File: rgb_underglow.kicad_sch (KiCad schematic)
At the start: 33 parts, among them U8 74AHCT1G125

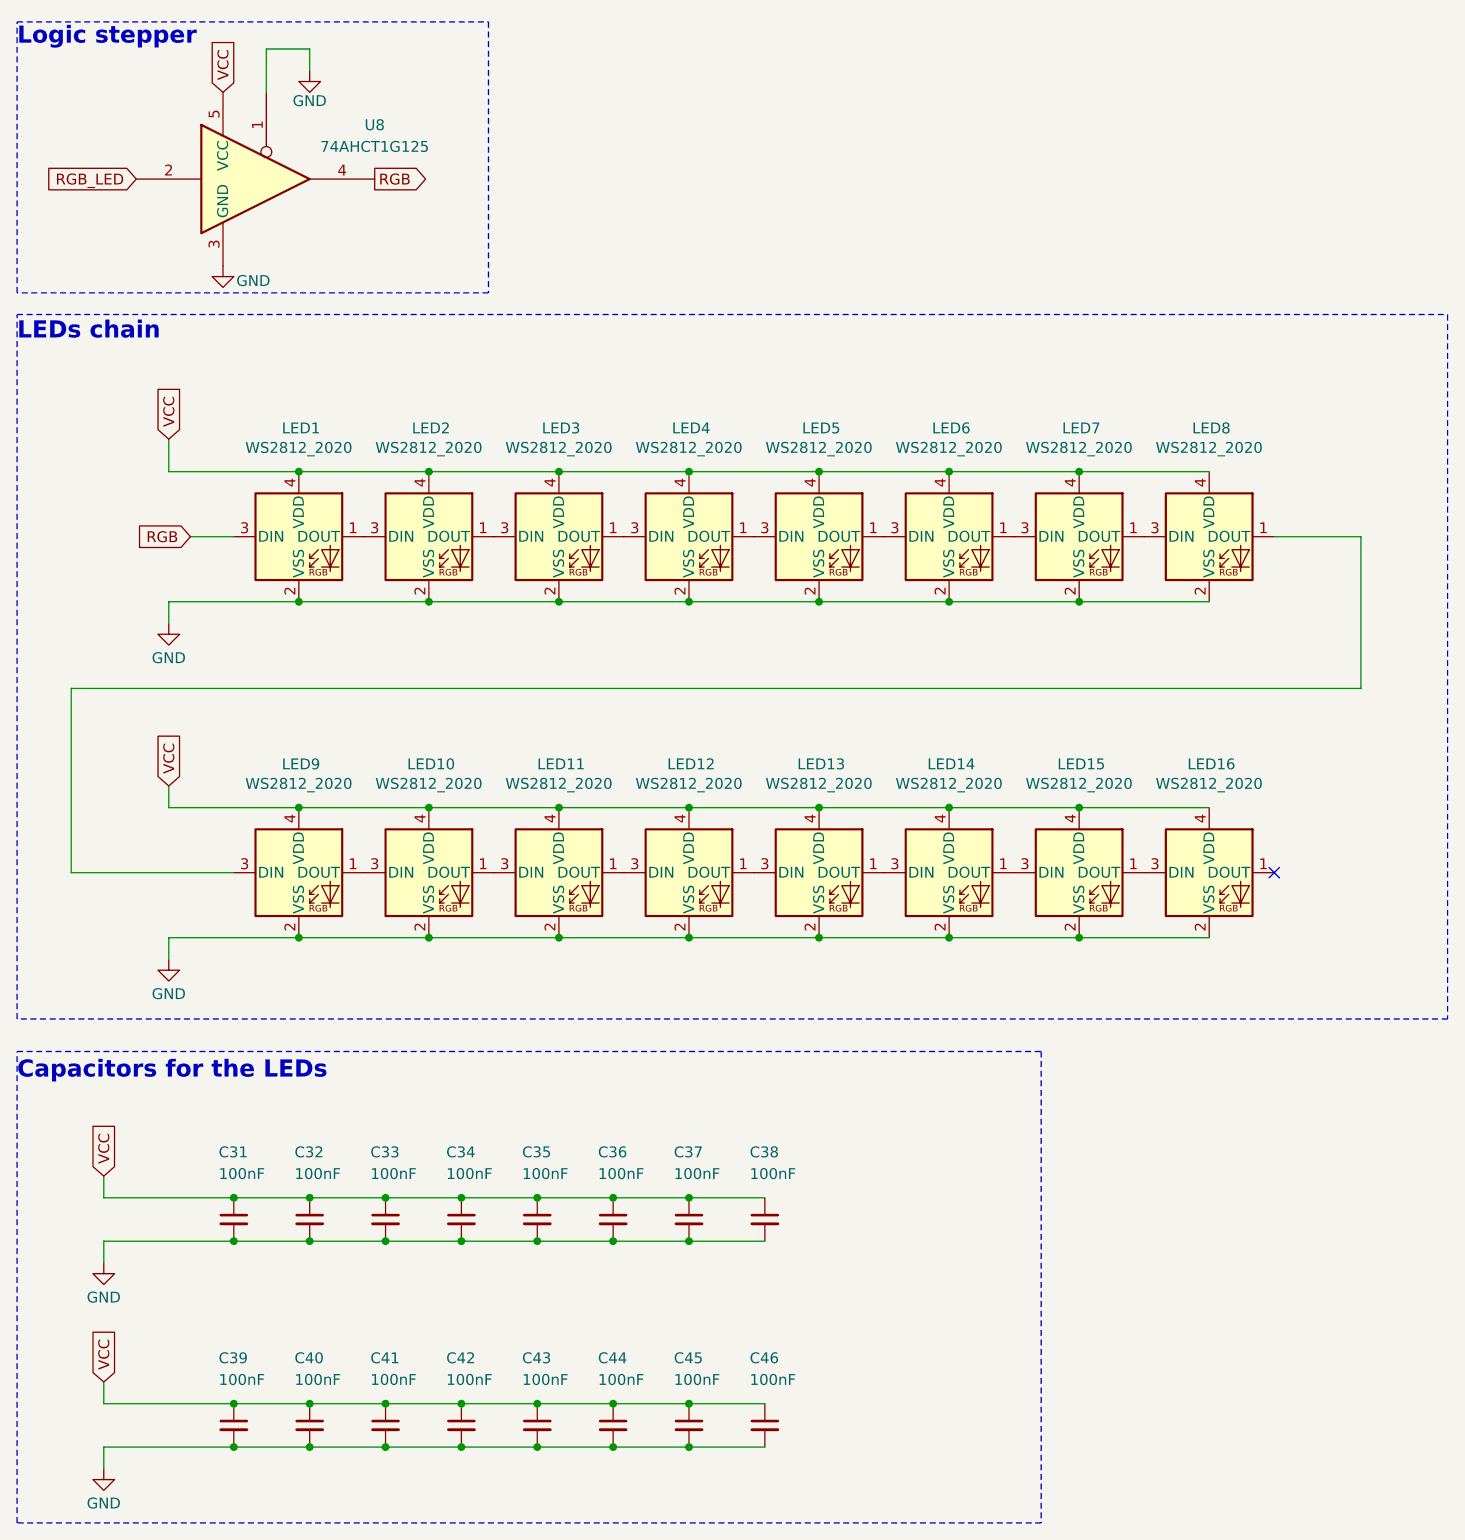
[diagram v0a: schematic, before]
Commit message: Changed USB type-A and LED parts
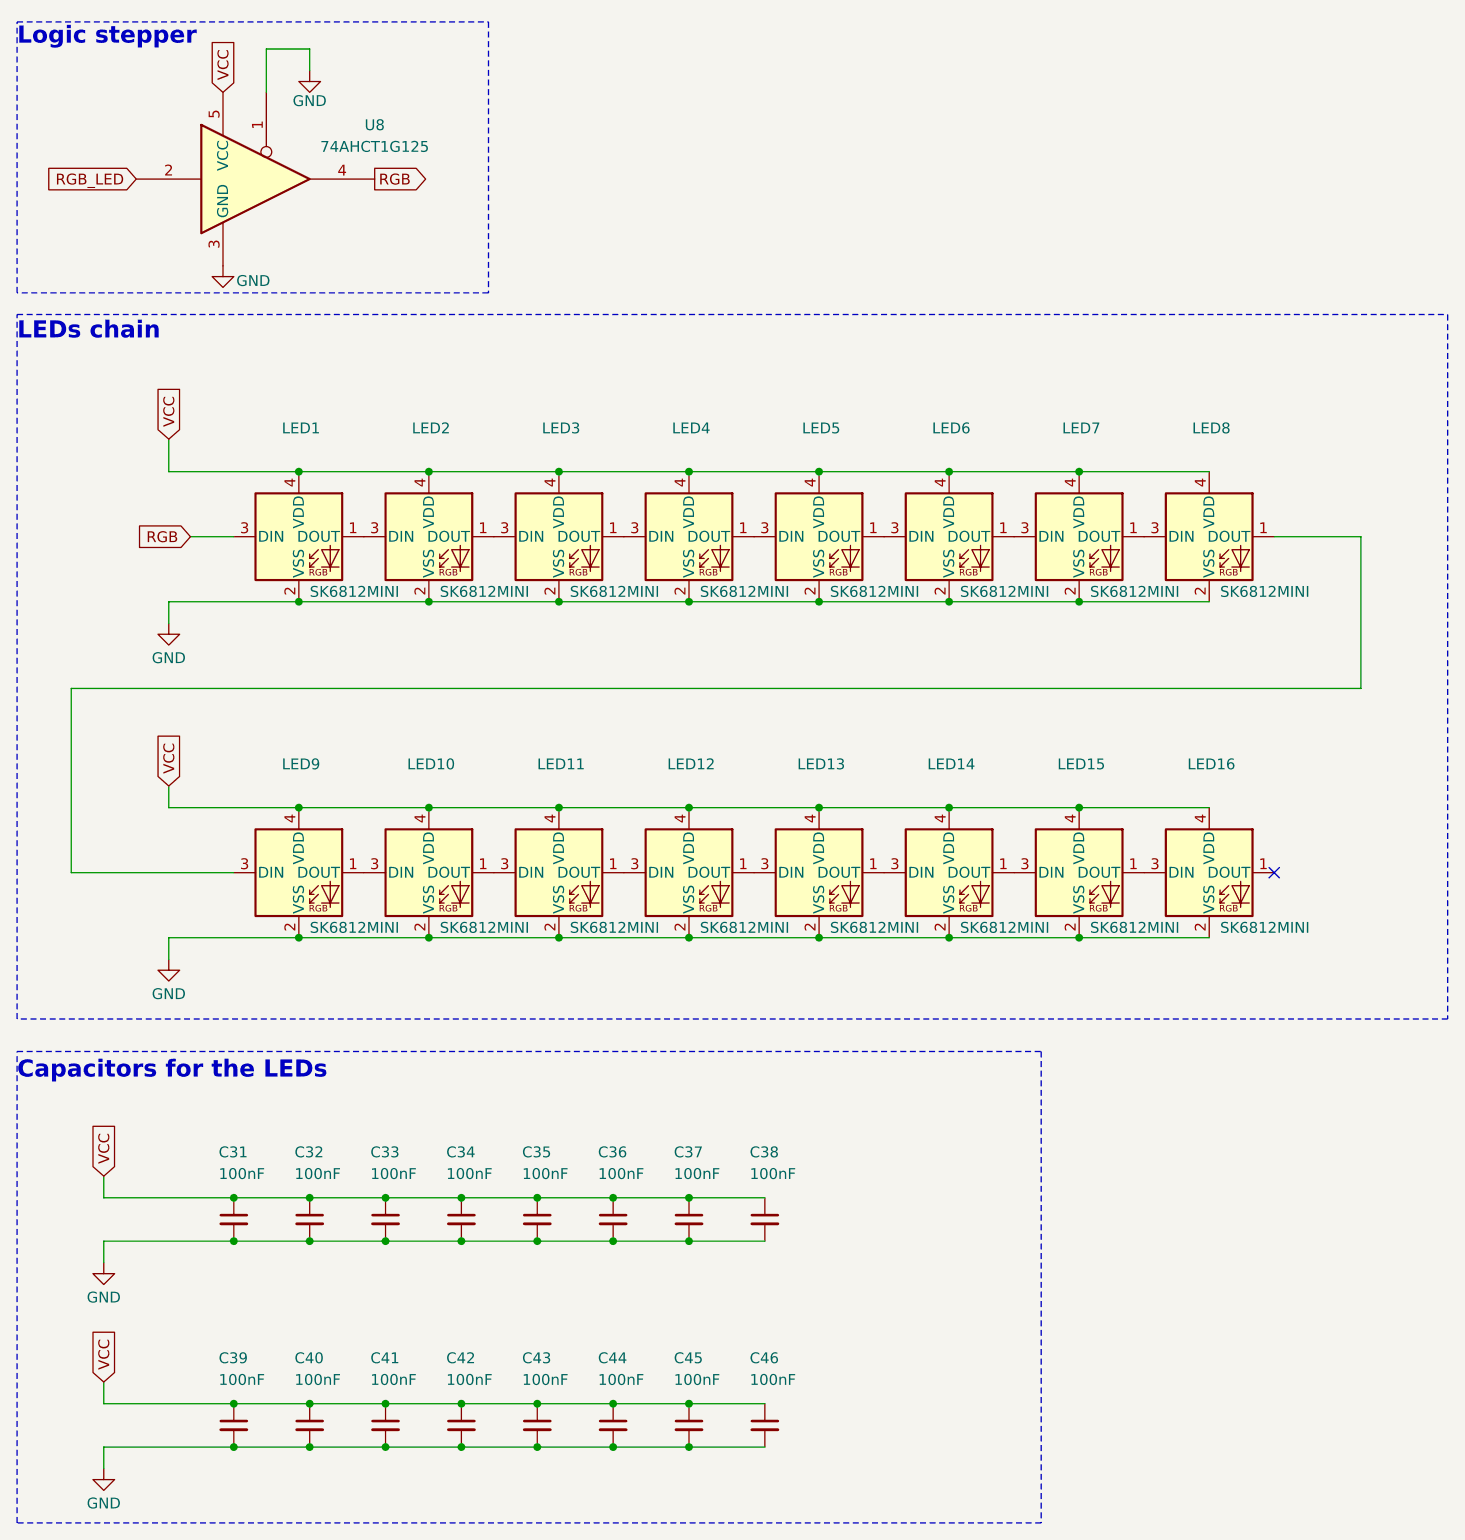
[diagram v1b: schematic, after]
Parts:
- LED1, LED10, LED11, LED12, LED13, LED14, LED15, LED16, LED2, LED3, LED4, LED5, LED6, LED7, LED8, LED9: value WS2812_2020 -> SK6812MINI; footprint PCM_marbastlib-various:LED_WS2812_2020 -> LED_SMD:LED_SK6812MINI_PLCC4_3.5x3.5mm_P1.75mm; symbol PCM_marbastlib-various:WS2812_2020 -> LED:SK6812MINI

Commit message: checking phase
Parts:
- LED1, LED10, LED11, LED12, LED13, LED14, LED15, LED16, LED2, LED3, LED4, LED5, LED6, LED7, LED8, LED9: footprint LED_SMD:LED_SK6812MINI_PLCC4_3.5x3.5mm_P1.75mm -> LED_SK6812MINI_HS:LED_SK6812MINI_HAND_SOLDER_3.5x3.5mm_P1.75mm
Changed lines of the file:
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@@
 			)
 		)
-		(property "Footprint" "LED_SMD:LED_SK6812MINI_PLCC4_3.5x3.5mm_P1.75mm"
+		(property "Footprint" "LED_SK6812MINI_HS:LED_SK6812MINI_HAND_SOLDER_3.5x3.5mm_P1.75mm"
 			(at 139.7 121.92 0)
 			(effects
@@
 			)
 		)
-		(property "Footprint" "LED_SMD:LED_SK6812MINI_PLCC4_3.5x3.5mm_P1.75mm"
+		(property "Footprint" "LED_SK6812MINI_HS:LED_SK6812MINI_HAND_SOLDER_3.5x3.5mm_P1.75mm"
 			(at 93.98 82.55 0)
 			(effects
@@
 			)
 		)
-		(property "Footprint" "LED_SMD:LED_SK6812MINI_PLCC4_3.5x3.5mm_P1.75mm"
+		(property "Footprint" "LED_SK6812MINI_HS:LED_SK6812MINI_HAND_SOLDER_3.5x3.5mm_P1.75mm"
 			(at 48.26 121.92 0)
 			(effects
@@
 			)
 		)
-		(property "Footprint" "LED_SMD:LED_SK6812MINI_PLCC4_3.5x3.5mm_P1.75mm"
+		(property "Footprint" "LED_SK6812MINI_HS:LED_SK6812MINI_HAND_SOLDER_3.5x3.5mm_P1.75mm"
 			(at 109.22 82.55 0)
 			(effects
@@
 			)
 		)
-		(property "Footprint" "LED_SMD:LED_SK6812MINI_PLCC4_3.5x3.5mm_P1.75mm"
+		(property "Footprint" "LED_SK6812MINI_HS:LED_SK6812MINI_HAND_SOLDER_3.5x3.5mm_P1.75mm"
 			(at 63.5 121.92 0)
 			(effects
@@
 			)
 		)
-		(property "Footprint" "LED_SMD:LED_SK6812MINI_PLCC4_3.5x3.5mm_P1.75mm"
+		(property "Footprint" "LED_SK6812MINI_HS:LED_SK6812MINI_HAND_SOLDER_3.5x3.5mm_P1.75mm"
 			(at 93.98 121.92 0)
 			(effects
@@
 			)
 		)
-		(property "Footprint" "LED_SMD:LED_SK6812MINI_PLCC4_3.5x3.5mm_P1.75mm"
+		(property "Footprint" "LED_SK6812MINI_HS:LED_SK6812MINI_HAND_SOLDER_3.5x3.5mm_P1.75mm"
 			(at 154.94 82.55 0)
 			(effects
@@
 			)
 		)
-		(property "Footprint" "LED_SMD:LED_SK6812MINI_PLCC4_3.5x3.5mm_P1.75mm"
+		(property "Footprint" "LED_SK6812MINI_HS:LED_SK6812MINI_HAND_SOLDER_3.5x3.5mm_P1.75mm"
 			(at 124.46 82.55 0)
 			(effects
@@
 			)
 		)
-		(property "Footprint" "LED_SMD:LED_SK6812MINI_PLCC4_3.5x3.5mm_P1.75mm"
+		(property "Footprint" "LED_SK6812MINI_HS:LED_SK6812MINI_HAND_SOLDER_3.5x3.5mm_P1.75mm"
 			(at 109.22 121.92 0)
 			(effects
@@
 			)
 		)
-		(property "Footprint" "LED_SMD:LED_SK6812MINI_PLCC4_3.5x3.5mm_P1.75mm"
+		(property "Footprint" "LED_SK6812MINI_HS:LED_SK6812MINI_HAND_SOLDER_3.5x3.5mm_P1.75mm"
 			(at 48.26 82.55 0)
 			(effects
@@
 			)
 		)
-		(property "Footprint" "LED_SMD:LED_SK6812MINI_PLCC4_3.5x3.5mm_P1.75mm"
+		(property "Footprint" "LED_SK6812MINI_HS:LED_SK6812MINI_HAND_SOLDER_3.5x3.5mm_P1.75mm"
 			(at 124.46 121.92 0)
 			(effects
@@
 			)
 		)
-		(property "Footprint" "LED_SMD:LED_SK6812MINI_PLCC4_3.5x3.5mm_P1.75mm"
+		(property "Footprint" "LED_SK6812MINI_HS:LED_SK6812MINI_HAND_SOLDER_3.5x3.5mm_P1.75mm"
 			(at 63.5 82.55 0)
 			(effects
@@
 			)
 		)
-		(property "Footprint" "LED_SMD:LED_SK6812MINI_PLCC4_3.5x3.5mm_P1.75mm"
+		(property "Footprint" "LED_SK6812MINI_HS:LED_SK6812MINI_HAND_SOLDER_3.5x3.5mm_P1.75mm"
 			(at 154.94 121.92 0)
 			(effects
@@
 			)
 		)
-		(property "Footprint" "LED_SMD:LED_SK6812MINI_PLCC4_3.5x3.5mm_P1.75mm"
+		(property "Footprint" "LED_SK6812MINI_HS:LED_SK6812MINI_HAND_SOLDER_3.5x3.5mm_P1.75mm"
 			(at 139.7 82.55 0)
 			(effects
@@
 			)
 		)
-		(property "Footprint" "LED_SMD:LED_SK6812MINI_PLCC4_3.5x3.5mm_P1.75mm"
+		(property "Footprint" "LED_SK6812MINI_HS:LED_SK6812MINI_HAND_SOLDER_3.5x3.5mm_P1.75mm"
 			(at 78.74 121.92 0)
 			(effects
@@
 			)
 		)
-		(property "Footprint" "LED_SMD:LED_SK6812MINI_PLCC4_3.5x3.5mm_P1.75mm"
+		(property "Footprint" "LED_SK6812MINI_HS:LED_SK6812MINI_HAND_SOLDER_3.5x3.5mm_P1.75mm"
 			(at 78.74 82.55 0)
 			(effects
